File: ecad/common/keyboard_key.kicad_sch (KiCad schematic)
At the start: 4 parts, among them SW4 SW_Push

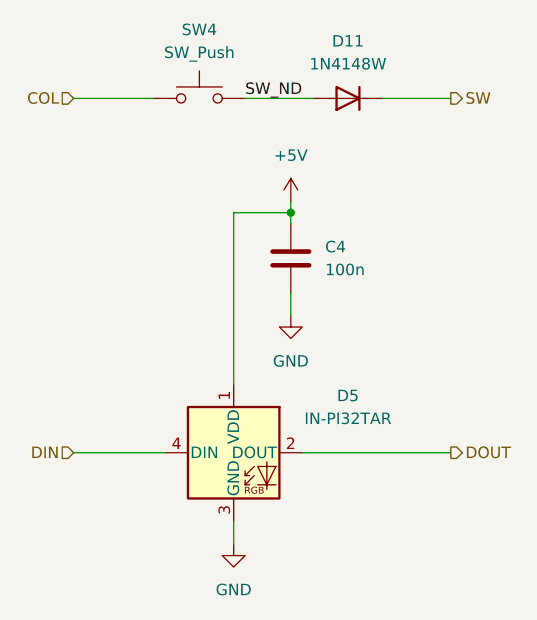
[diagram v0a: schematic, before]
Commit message: Draft a slightly smaller top board
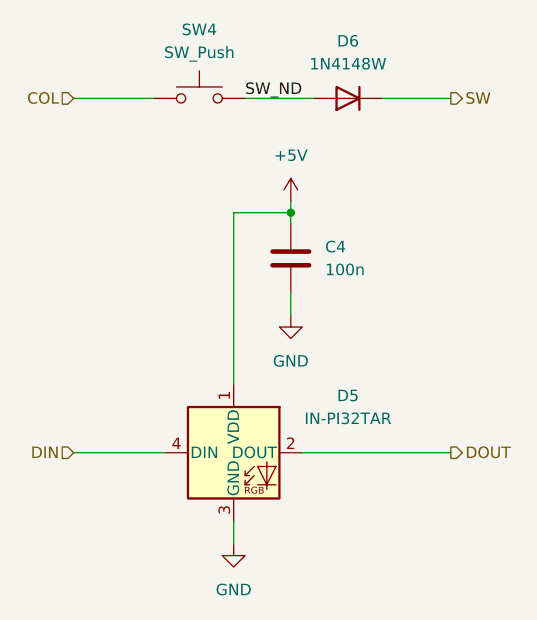
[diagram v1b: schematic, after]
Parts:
- renumbered D11 to D6
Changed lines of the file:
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@@
 		(dnp no)
 		(fields_autoplaced yes)
-		(property "Reference" "D11"
+		(property "Reference" "D6"
 			(at 110.49 25.4 0)
 			(effects

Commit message: Adds a bottom section
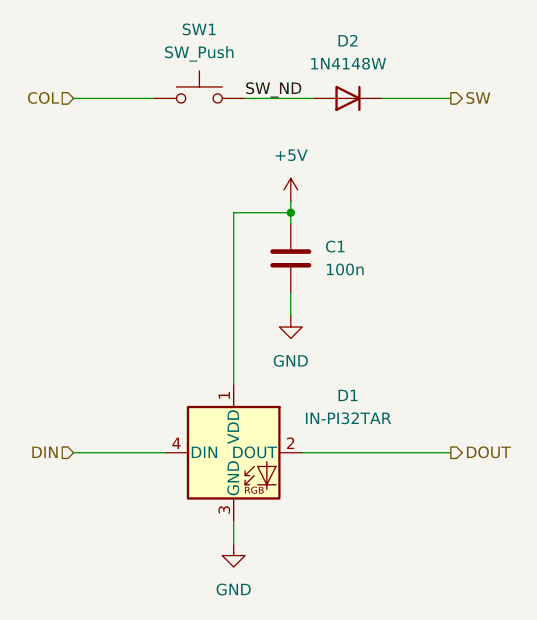
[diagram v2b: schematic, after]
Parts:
- renumbered C4 to C1, D5 to D1, D6 to D2, SW4 to SW1

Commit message: Adds a bottom_section board.
It was fast. Seems the right design choices.
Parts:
- renumbered C1 to C9, D1 to D17, D2 to D18, SW1 to SW9
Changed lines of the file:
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@@
 		(on_board yes)
 		(dnp no)
-		(property "Reference" "D1"
+		(property "Reference" "D17"
 			(at 110.49 64.8014 0)
 			(effects
@@
 		(on_board yes)
 		(dnp no)
-		(property "Reference" "#PWR02"
+		(property "Reference" "#PWR026"
 			(at 104.14 46.99 0)
 			(effects
@@
 		(on_board yes)
 		(dnp no)
-		(property "Reference" "SW1"
+		(property "Reference" "SW9"
 			(at 93.98 24.13 0)
 			(effects
@@
 		(dnp no)
 		(fields_autoplaced yes)
-		(property "Reference" "#PWR01"
+		(property "Reference" "#PWR025"
 			(at 97.79 87.63 0)
 			(effects
@@
 		(dnp no)
 		(fields_autoplaced yes)
-		(property "Reference" "C1"
+		(property "Reference" "C9"
 			(at 107.95 48.2599 0)
 			(effects
@@
 		(dnp no)
 		(fields_autoplaced yes)
-		(property "Reference" "#PWR03"
+		(property "Reference" "#PWR027"
 			(at 104.14 62.23 0)
 			(effects
@@
 		(dnp no)
 		(fields_autoplaced yes)
-		(property "Reference" "D2"
+		(property "Reference" "D18"
 			(at 110.49 25.4 0)
 			(effects

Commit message: Updates boards
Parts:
- renumbered C9 to C2, D17 to D2, D18 to D3, SW9 to SW2

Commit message: Uses WS2811 led communication everywhere
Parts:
- D2: MPN (none) -> IN-PI32TARPRPGPB
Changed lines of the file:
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@@
 (kicad_sch
-	(version 20231120)
+	(version 20250114)
 	(generator "eeschema")
-	(generator_version "8.0")
+	(generator_version "9.0")
 	(paper "A5")
 	(junction
@@
 	(label "SW_ND"
 		(at 99.06 31.75 0)
-		(fields_autoplaced yes)
 		(effects
 			(font
@@
 		(shape input)
 		(at 80.01 71.12 180)
-		(fields_autoplaced yes)
 		(effects
 			(font
@@
 		(shape output)
 		(at 121.92 31.75 0)
-		(fields_autoplaced yes)
 		(effects
 			(font
@@
 		(shape output)
 		(at 121.92 71.12 0)
-		(fields_autoplaced yes)
 		(effects
 			(font
@@
 		(shape input)
 		(at 80.01 31.75 180)
-		(fields_autoplaced yes)
 		(effects
 			(font
@@
 			(effects
 				(font
+					(size 1.27 1.27)
+				)
+				(hide yes)
+			)
+		)
+		(property "MPN" "IN-PI32TARPRPGPB"
+			(at 97.79 71.12 0)
+			(effects
+				(font

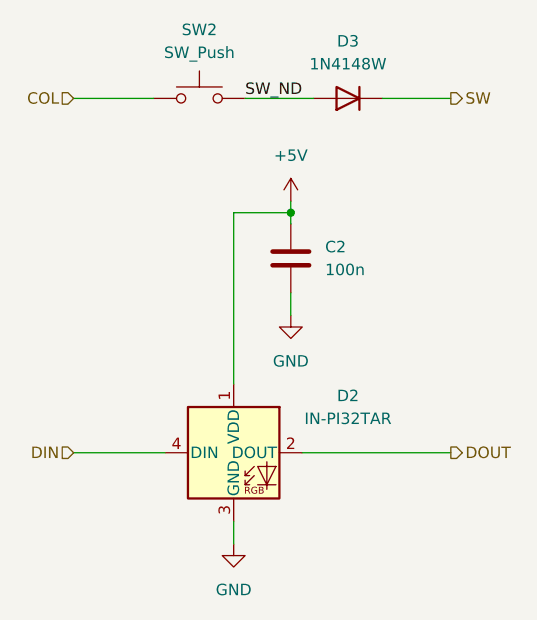
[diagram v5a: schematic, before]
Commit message: Uses attiny16176
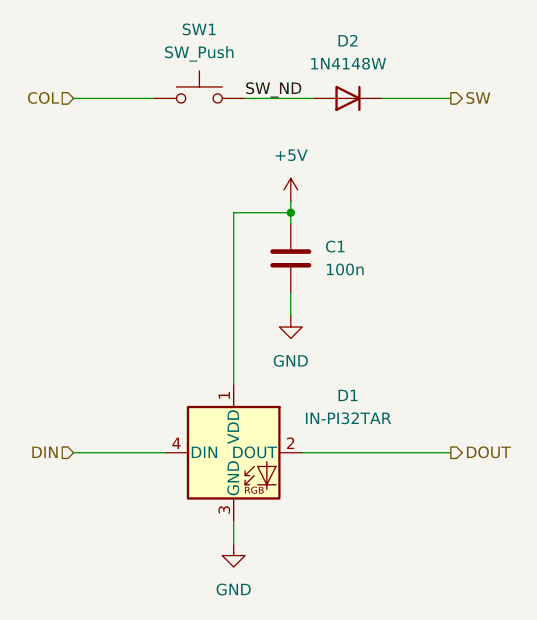
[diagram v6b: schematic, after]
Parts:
- renumbered C2 to C1, D2 to D1, D3 to D2, SW2 to SW1
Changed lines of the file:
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@@
 		(on_board yes)
 		(dnp no)
-		(property "Reference" "D2"
+		(property "Reference" "D1"
 			(at 110.49 64.8014 0)
 			(effects
@@
 		(on_board yes)
 		(dnp no)
-		(property "Reference" "#PWR0108"
+		(property "Reference" "#PWR02"
 			(at 104.14 46.99 0)
 			(effects
@@
 		(on_board yes)
 		(dnp no)
-		(property "Reference" "SW2"
+		(property "Reference" "SW1"
 			(at 93.98 24.13 0)
 			(effects
@@
 		(dnp no)
 		(fields_autoplaced yes)
-		(property "Reference" "#PWR0109"
+		(property "Reference" "#PWR01"
 			(at 97.79 87.63 0)
 			(effects
@@
 		(dnp no)
 		(fields_autoplaced yes)
-		(property "Reference" "C2"
+		(property "Reference" "C1"
 			(at 107.95 48.2599 0)
 			(effects
@@
 		(dnp no)
 		(fields_autoplaced yes)
-		(property "Reference" "#PWR0107"
+		(property "Reference" "#PWR03"
 			(at 104.14 62.23 0)
 			(effects
@@
 		(dnp no)
 		(fields_autoplaced yes)
-		(property "Reference" "D3"
+		(property "Reference" "D2"
 			(at 110.49 25.4 0)
 			(effects

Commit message: [WIP] Control board
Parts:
- renumbered C1 to C2, D1 to D2, D2 to D3, SW1 to SW2
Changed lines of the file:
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@@
 		(on_board yes)
 		(dnp no)
-		(property "Reference" "D1"
+		(property "Reference" "D2"
 			(at 110.49 64.8014 0)
 			(effects
@@
 		(on_board yes)
 		(dnp no)
-		(property "Reference" "#PWR02"
+		(property "Reference" "#PWR0108"
 			(at 104.14 46.99 0)
 			(effects
@@
 		(on_board yes)
 		(dnp no)
-		(property "Reference" "SW1"
+		(property "Reference" "SW2"
 			(at 93.98 24.13 0)
 			(effects
@@
 		(dnp no)
 		(fields_autoplaced yes)
-		(property "Reference" "#PWR01"
+		(property "Reference" "#PWR0109"
 			(at 97.79 87.63 0)
 			(effects
@@
 		(dnp no)
 		(fields_autoplaced yes)
-		(property "Reference" "C1"
+		(property "Reference" "C2"
 			(at 107.95 48.2599 0)
 			(effects
@@
 		(dnp no)
 		(fields_autoplaced yes)
-		(property "Reference" "#PWR03"
+		(property "Reference" "#PWR0107"
 			(at 104.14 62.23 0)
 			(effects
@@
 		(dnp no)
 		(fields_autoplaced yes)
-		(property "Reference" "D2"
+		(property "Reference" "D3"
 			(at 110.49 25.4 0)
 			(effects

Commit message: WIP LED
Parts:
- removed C2: 100n, Capacitor_SMD:C_0603_1608Metric, symbol Device:C
- removed D2: IN-PI32TAR, woodpecker:LED_Inolux_IN-PI32TAR_PLCC4_3.2x2.8mm_P1.5mm, symbol woodpecker:Inolux_IN-PI32TAR
- added D: LED_BGRA, symbol Device:LED_BGRA
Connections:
- new net LEDA: D.4 (A)
- new net LEDB: D.1 (BK)
- new net LEDG: D.2 (GK)
- new net LEDR: D.3 (RK)
